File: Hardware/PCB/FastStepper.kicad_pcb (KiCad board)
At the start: 4 copper layers, 61.9 x 84.4 mm, 138 parts, among them IC1 FT232RL, IC10 THS4281DBVT, IC11 M74VHC1GT126DT1G, IC13 M74VHC1GT126DT1G, IC14 M74VHC1GT126DT1G, IC15 M74VHC1GT126DT1G, IC16 M74VHC1GT126DT1G, IC17 M74VHC1GT126DT1G, IC18 M74VHC1GT126DT1G, IC19 M74VHC1GT126DT1G, IC2 M74VHC1GT126DT1G, IC20 M74VHC1GT126DT1G, IC21 M74VHC1GT126DT1G, IC22 M74VHC1GT126DT1G, IC3 LP5907MFX-3.3, IC4 M74VHC1GT126DT1G, IC5 M74VHC1GT126DT1G, IC6 M74VHC1GT126DT1G, IC8 ATXMEGA32A4U, J1 USB_C_Receptacle, J2 PJ-316A-6A, J3 PJ-316A-6A, J4 Keystone 8734, J6 Keystone 8734, Q1 AO3401A, U1 74LVC1G157, U2 THVD1450D, U3 ADUM1201BRZ, X1 conn 1x5 2, X10 conn 1x3, X2 conn 1x5, X3 conn 1x2, X4 conn 1x3, X5 conn 1x5, X6 OSCILLATOR, X9 conn 1x5

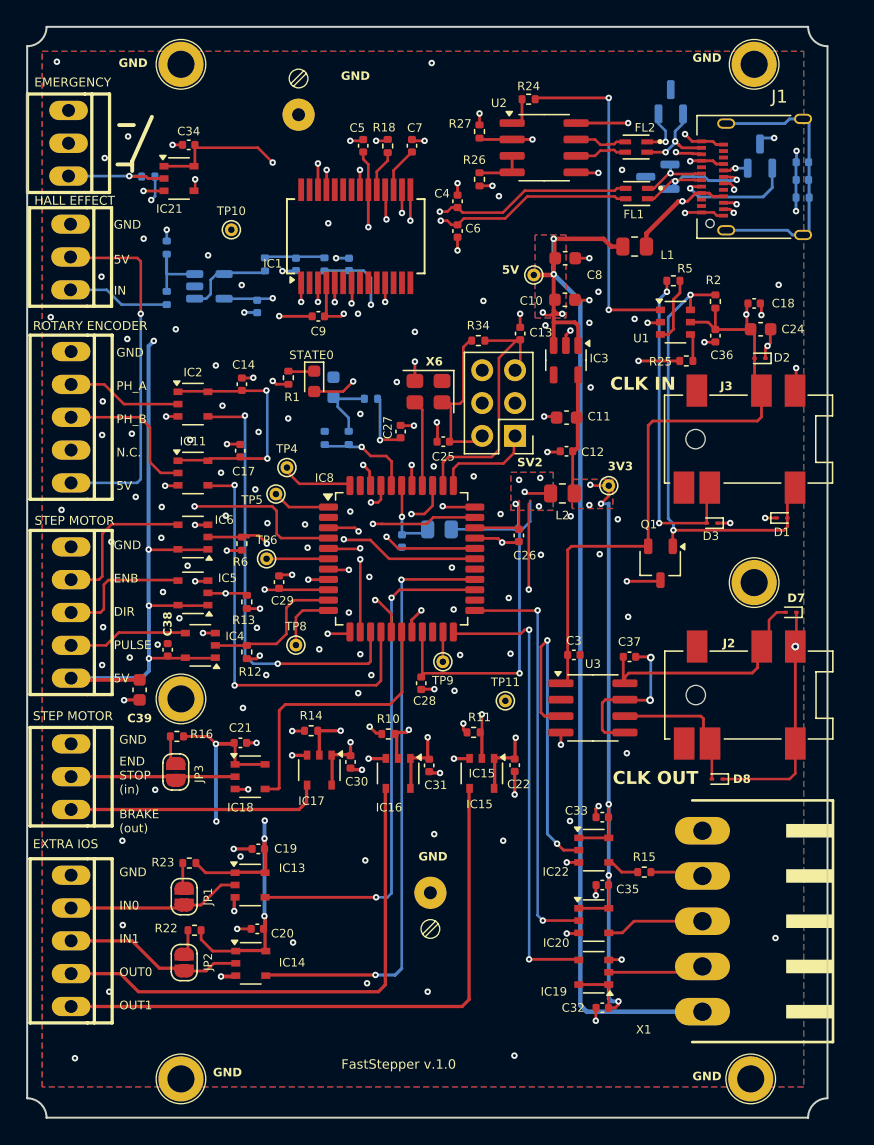
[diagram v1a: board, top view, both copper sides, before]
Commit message: fine tunning
- fine position adjust on X1 plug
- Top & Bott Fabrication Layers 'cleaned' - can be used on production
- generated new Gerbers & Drill files
- BOM & Pick&Place stand as it were
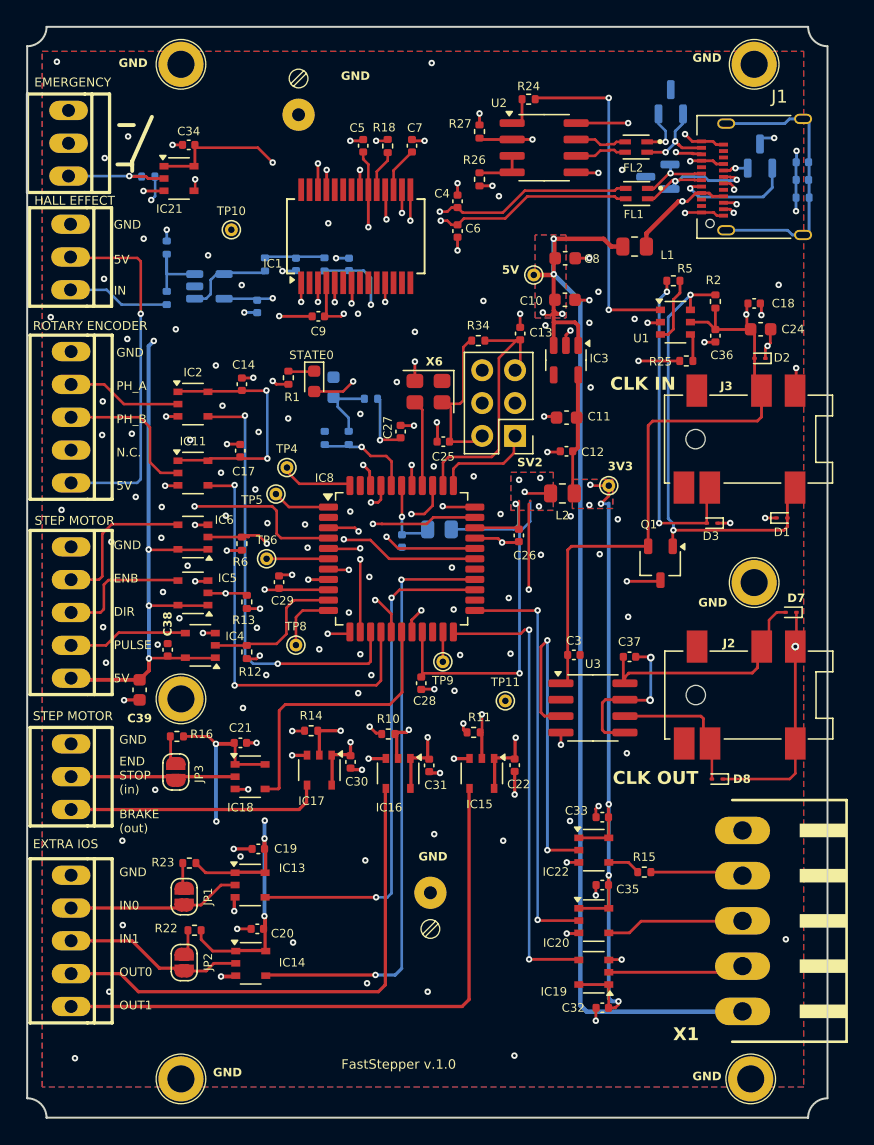
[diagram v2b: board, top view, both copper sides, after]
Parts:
- X1: footprint FastStepper PCBLib:90G-5 -> FastStepper PCBLib:20_155MH_5
- moved X1 3.10 mm to (180.1, 133.8)
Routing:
- net /IO stage/2Harp_H2_RX: track 6.80 -> 10.4 mm
- net /IO stage/2Harp_ClockOut: track 3.69 -> 7.05 mm
- net /IO stage/2Harp_H2_TX: track 7.62 -> 10.6 mm
- net +5V: track 321.0 -> 318.7 mm
- net CLK_2u: track 75.4 -> 76.3 mm
- net GND: vias 161 -> 160

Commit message: tunning de tracks & vias por exegse da Eurocircuits
Para ser produzível por Eurocircuits:
- vias redimensionadas
- pequenos movimentos de movimentos de tracks & vias - não houve movimento componentes
- gerados Gerbers & PTH & NPTH
- P&P como estava
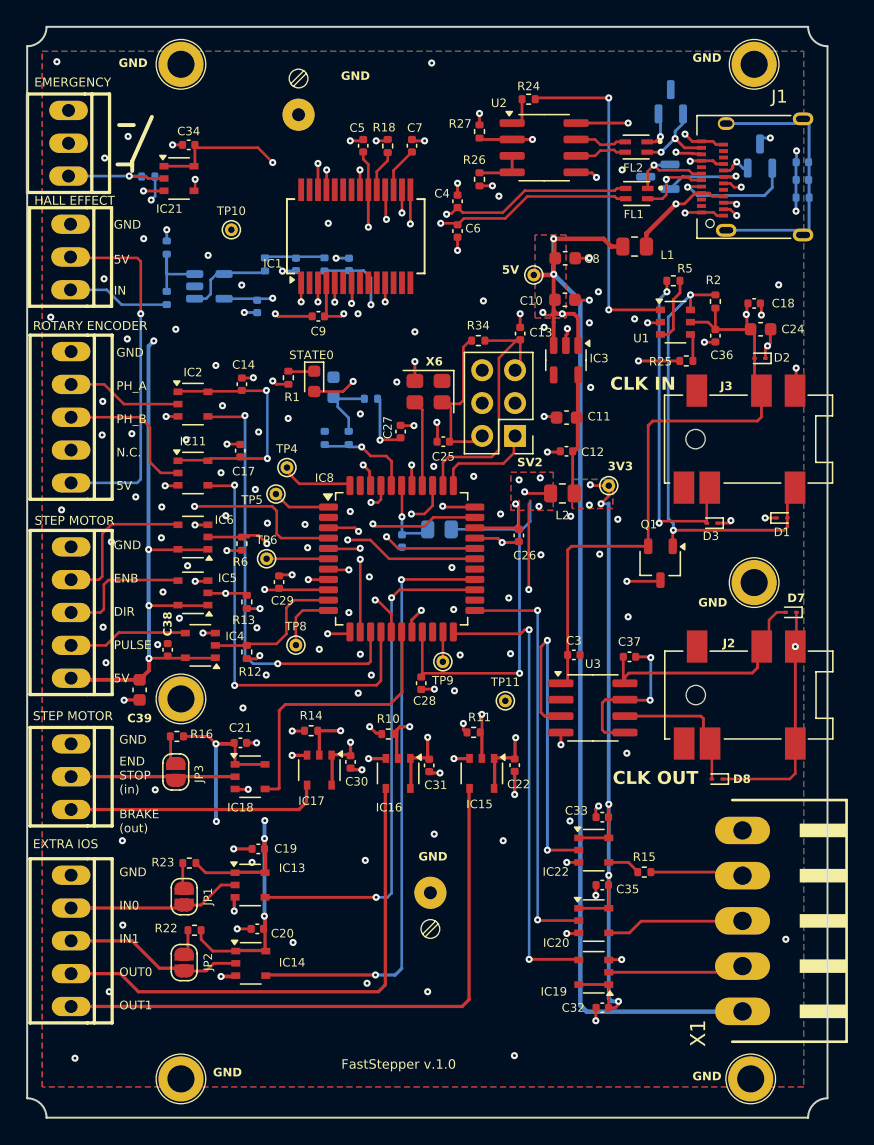
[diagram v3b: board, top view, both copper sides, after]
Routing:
- net /USB_N: track 11.9 -> 16.2 mm
- net /Clock stage/~{CLCK_DET}: track 36.8 -> 35.1 mm
- net VClk: track 77.7 -> 76.0 mm
- net Net-(D7-A2): track 18.5 -> 17.3 mm
- net /USB_CLCK_N: track 15.4 -> 16.6 mm
- net /Clock stage/CLCK_OUT: track 11.1 -> 10.2 mm
- net /IO stage/2Harp_H2_RX: track 10.4 -> 9.53 mm
- net /USB_P: track 12.4 -> 13.0 mm
- net /IO stage/2Harp_ClockOut: track 7.05 -> 6.42 mm
- net UC_OUTPUT0: track 22.4 -> 23.0 mm
